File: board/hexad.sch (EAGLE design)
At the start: 0 parts

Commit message: added more parts
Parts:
- added C1, C3: 47uF@50V, holla:C-POLARIZED-E-6
- added C10, C11, C2, C4: 1u, holla:C-0603
- added C5, C7, C8, C9: .1u, holla:C-0603
- added C6: DNP, holla:C-0603
- added D3: VZ10, holla:DIODE-ZENER-SOD323
- added D4: GRN, holla:LED-0603
- added J1, JCYCLE, JDOOR, JFEED: (no value), holla:CONN-02-3.81MM-PLUGIN-SCREW
- added J11: (no value), holla:CONN-MICROSD-2908-05WB-MG
- added J2: (no value), holla:CONN-04-.100-VERT-HEADER
- added J3: (no value), holla:DISP-SPI-TFT-128X160-ST7735
- added JA, JSPINDLE, JX, JY, JZ: (no value), holla:CONN-06-3.81MM-PLUGIN-SCREW
- added JP1, JP2: FIDUCIAL-MICRO, holla:FIDUCIAL-MICRO
- added Q1: 40V, holla:FET-PCH-SOT23
- added Q10, Q11, Q12, Q13, Q2, Q3, Q4, Q5, Q6, Q7, Q8, Q9: (no value), holla:FET-NCH-SOT23
- added R1: 100k, holla:R-0603
- added R10, R12, R16, R20, R22, R4, R7: 10k, holla:R-0603
- added R11, R15, R19, R21, R5, R8, R9: 100, holla:R-0603
- added R13, R14: 2k, holla:R-0603
- added R17, R18: DNP, holla:R-0603
- added R2, R3: (no value), holla:R-0603
- added R23, R6: 1k, holla:R-0603
- added S1: (no value), holla:SWITCH-PUSHBUTTON-EVQ5
- added TP1, TP2, TP3, TPG: (no value), holla:TESTPOINTTHRU
- added U1: RADIO-ESP32_DEVKIT, holla:RADIO-ESP32_DEVKIT
- added U2: R-78E5.0-1.0, holla:VREG-SIP3
- added U3: (no value), holla:IO-MCP23017SO
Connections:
- new net 24V0: C1.+, D3.C, JA.6, JSPINDLE.6, JX.6, JY.6, JZ.6, Q1.S, U2.VIN
- new net 3V3: C10.2, C2.2, C4.2, J11.VDD, Q2.G, R10.2, R12.2, R13.2, R14.2, R16.2, R18.2, R20.2, R22.2, R23.2, R3.2, R4.2, R7.2, U1.3V3, U3.VDD
- new net 5V0: C3.+, JA.5, JSPINDLE.5, JX.5, JY.5, JZ.5, R2.2, R6.2, U1.VIN, U2.VOUT
- new net A_DIR: Q10.G, U1.D2
- new net A_LIMIT: C9.1, R11.2, U1.D4
- new net A_STEP: Q9.G, U1.D15
- new net CS_SD: J11.CS, U1.D34
- new net CYCLE_START: R21.2, U1.VN/AD3/D39
- new net DOOR: R15.2
- new net FEED_HOLD: R19.2, U1.VP/AD0/D36
- new net GND: C1.-, C10.1, C11.1, C2.1, C3.-, C4.1, C5.2, C6.2, C7.2, C8.2, C9.2, D4.C, J1.1, J11.GND, J11.GND1, J11.VSS, J3.GND, JA.1, JCYCLE.1, JDOOR.1, JFEED.1, JSPINDLE.1, JX.1, JY.1, JZ.1, Q10.S, Q11.S, Q12.S, Q13.S, Q3.S, Q4.S, Q5.S, Q6.S, Q7.S, Q8.S, Q9.S, R1.1, S1.1, TPG.P$1, U1.GND@1, U1.GND@2, U2.GND, U3.A0, U3.A1, U3.A2, U3.VSS
- new net MISO: J11.DATA_OUT, TP2.P$1, U1.D19
- new net MOSI: J11.DATA_IN, TP1.P$1, U1.D23
- new net N$1: J1.2, Q1.D
- new net N$10: JA.4, R11.1, R12.1
- new net N$11: JA.2, Q10.D
- new net N$12: JDOOR.2, R15.1, R16.1
- new net N$13: JSPINDLE.4, Q13.D, R17.1, R18.1
- new net N$14: JSPINDLE.2, Q12.D
- new net N$15: J3.RESET
- new net N$16: JFEED.2, R19.1, R20.1
- new net N$17: JCYCLE.2, R21.1, R22.1
- new net N$18: J2.4
- new net N$19: J2.3
- new net N$2: JX.4, R4.1, R8.1
- new net N$20: J2.2
- new net N$21: J2.1
- new net N$22: J3.MOSI
- new net N$23: J3.SCLK
- new net N$24: D3.A, Q1.G, R1.2
- new net N$25: J3.VCC
- new net N$26: J3.CS
- new net N$3: Q2.S, R3.1
- new net N$4: Q2.D, R2.1
- new net N$5: JX.2, Q4.D
- new net N$6: JY.4, R5.1, R7.1
- new net N$7: JY.2, Q6.D
- new net N$8: JZ.4, R10.1, R9.1
- new net N$84: D4.A, R6.1
- new net N$9: JZ.2, Q8.D
- new net RESET: C11.2, R23.1, S1.2, U1.EN, U3.!RESET
- new net SCK: J11.SCLK, TP3.P$1, U1.D18
- new net SCL: R14.1, U1.D22, U3.SCL
- new net SDA: R13.1, U1.D21, U3.SDA
- new net SPINDLE_DIR: Q12.G, U1.D17/TX2
- new net SPINDLE_ENABLE: C6.1, Q13.G, R17.2, U1.D5
- new net SPINDLE_PWM: Q11.G, U1.D16/RX2
- new net X_DIR: Q4.G, U1.D12
- new net X_LIMIT: C5.1, R8.2, U1.D14
- new net X_STEP: Q3.G, U1.D13
- new net X_STEP_5V0: JX.3, Q3.D
- new net X_STEP_5V1: JY.3, Q5.D
- new net X_STEP_5V2: JZ.3, Q7.D
- new net X_STEP_5V3: JA.3, Q9.D
- new net X_STEP_5V4: JSPINDLE.3, Q11.D
- new net Y_DIR: Q6.G, U1.D26
- new net Y_LIMIT: C7.1, R5.2, U1.D25
- new net Y_STEP: Q5.G, U1.D27
- new net Z_DIR: Q8.G, U1.D32
- new net Z_LIMIT: C8.1, R9.2, U1.D35
- new net Z_STEP: Q7.G, U1.D33
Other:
- note added: "add ST7735 display connector"

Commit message: started routing
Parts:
- removed J3: (no value), holla:DISP-SPI-TFT-128X160-ST7735
- removed JDOOR: (no value), holla:CONN-02-3.81MM-PLUGIN-SCREW
- removed S1: (no value), holla:SWITCH-PUSHBUTTON-EVQ5
- removed TP1, TP2, TP3: (no value), holla:TESTPOINTTHRU
- added 24V0, 3V3, 5V0, MISO, MOSI, SCK: (no value), holla:TESTPOINTTHRU
- added C12, C13, C14, C15: .1u, holla:C-0603
- added DISPLAY: (no value), holla:DISP-SPI-TFT-128X160-ST7735
- added J24V0, J3V3, J5V0, LED0, LED1, LED2, LED3, RESET, USER0, USER1, USER2, USER3: (no value), holla:CONN-02-.100-VERT-HEADER
- added R24, R25: 220, holla:R-0603
- added R26, R27: 100, holla:R-0603
- Q1: device holla:FET-PCH-SOT23 -> holla:FET-PCH-TO252
- R15: value 100 -> 220
- R16: value 10k -> 220
- renumbered J1 to VIN, J2 to I2C, JA to A, JCYCLE to CYCLE, JFEED to FEED, JSPINDLE to SPINDLE, JX to X, JY to Y, JZ to Z
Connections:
- removed net DOOR: R15.2
- removed net N$21: I2C.1
- new net DISPLAY_CS: DISPLAY.CS, U3.GPA4
- new net DISPLAY_DC: DISPLAY.DC, U3.GPA5
- new net N$27: LED2.2, R24.2
- new net N$28: LED1.2, R16.2
- new net N$29: LED0.2, R15.2
- new net USER0: C12.1, U3.GPB0, USER0.2
- new net USER1: C13.1, U3.GPB1, USER1.2
- new net USER2: C14.1, U3.GPB2, USER2.2
- new net USER3: C15.1, U3.GPB3, USER3.2
- net 24V0: now also 24V0.P$1, J24V0.2
- net 3V3: now also 3V3.P$1, J3V3.2; no longer R16.2
- net 5V0: now also 5V0.P$1, I2C.2, J5V0.2
- net GND: now also C12.2, C13.2, C14.2, C15.2, DISPLAY.GND, I2C.1, J24V0.1, J3V3.1, J5V0.1, LED0.1, LED1.1, LED2.1, LED3.1, RESET.1, USER0.1, USER1.1, USER2.1, USER3.1; no longer J3.GND, JDOOR.1, S1.1
- net MISO: now also MISO.P$1; no longer TP2.P$1
- net MOSI: now also DISPLAY.MOSI, MOSI.P$1; no longer TP1.P$1
- net N$12: now also U3.GPA0; no longer JDOOR.2, R16.1
- net N$15: now also R16.1, U3.GPA1; no longer J3.RESET
- net N$18: now also R27.1
- net N$19: now also R26.1
- net N$20: now also DISPLAY.BL; no longer I2C.2
- net N$22: now also R24.1, U3.GPA2; no longer J3.MOSI
- net N$23: now also R25.1, U3.GPA3; no longer J3.SCLK
- net N$25: now also DISPLAY.VCC; no longer J3.VCC
- net N$26: now also LED3.2, R25.2; no longer J3.CS
- net RESET: now also DISPLAY.RESET, RESET.2; no longer S1.2
- net SCK: now also DISPLAY.SCLK, SCK.P$1; no longer TP3.P$1
- net SCL: now also R27.2
- net SDA: now also R26.2
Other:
- note removed: "add ST7735 display connector"
- moved on the sheet: C11, R15, R16, R23, U1, U3

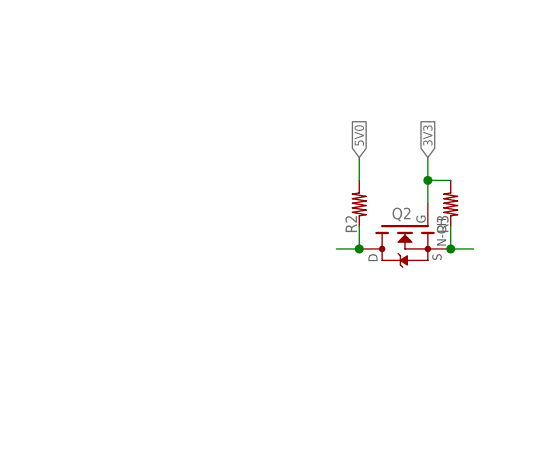
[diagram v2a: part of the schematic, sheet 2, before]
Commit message: changed connectors to 0.1 headers
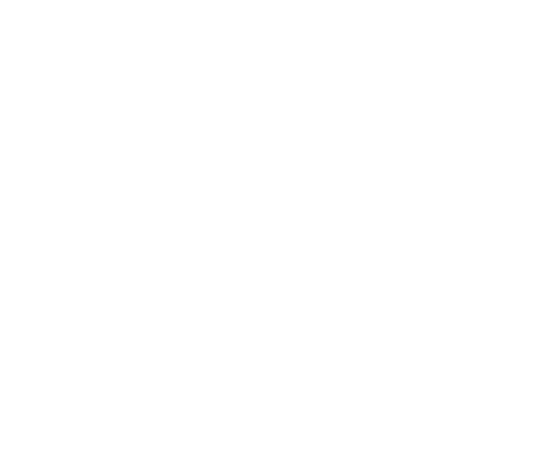
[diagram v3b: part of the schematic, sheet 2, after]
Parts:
- removed 24V0, 5V0: (no value), holla:TESTPOINTTHRU
- removed Q2: (no value), holla:FET-NCH-SOT23
- removed R2, R3: (no value), holla:R-0603
- A, SPINDLE, X, Y, Z: device holla:CONN-06-3.81MM-PLUGIN-SCREW -> holla:CONN-06-.100-VERT-HEADER
- CYCLE, FEED: device holla:CONN-02-3.81MM-PLUGIN-SCREW -> holla:CONN-02-.100-VERT-HEADER
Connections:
- removed net N$3: Q2.S, R3.1
- removed net N$4: Q2.D, R2.1
- net 24V0: no longer 24V0.P$1
- net 3V3: no longer Q2.G, R3.2
- net 5V0: no longer 5V0.P$1, R2.2
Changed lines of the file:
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@@
 <part name="GND2" library="holla" deviceset="GND" device=""/>
 <part name="GND4" library="holla" deviceset="GND" device=""/>
-<part name="X" library="holla" deviceset="CONN-06" device="-3.81MM-PLUGIN-SCREW"/>
-<part name="Q2" library="holla" deviceset="FET-NCH" device="-SOT23"/>
-<part name="R2" library="holla" deviceset="R" device="-0603"/>
-<part name="R3" library="holla" deviceset="R" device="-0603"/>
+<part name="X" library="holla" deviceset="CONN-06" device="-.100-VERT-HEADER"/>
 <part name="FRAME2" library="holla" deviceset="FRAME_A_L" device=""/>
 <part name="GND48" library="holla" deviceset="GND" device=""/>
@@
 <part name="R4" library="holla" deviceset="R" device="-0603" value="10k"/>
 <part name="GND5" library="holla" deviceset="GND" device=""/>
-<part name="Y" library="holla" deviceset="CONN-06" device="-3.81MM-PLUGIN-SCREW"/>
+<part name="Y" library="holla" deviceset="CONN-06" device="-.100-VERT-HEADER"/>
 <part name="R5" library="holla" deviceset="R" device="-0603" value="100"/>
 <part name="Q5" library="holla" deviceset="FET-NCH" device="-SOT23"/>
@@
 <part name="R7" library="holla" deviceset="R" device="-0603" value="10k"/>
 <part name="GND11" library="holla" deviceset="GND" device=""/>
-<part name="Z" library="holla" deviceset="CONN-06" device="-3.81MM-PLUGIN-SCREW"/>
+<part name="Z" library="holla" deviceset="CONN-06" device="-.100-VERT-HEADER"/>
 <part name="R9" library="holla" deviceset="R" device="-0603" value="100"/>
 <part name="Q7" library="holla" deviceset="FET-NCH" device="-SOT23"/>
@@
 <part name="R10" library="holla" deviceset="R" device="-0603" value="10k"/>
 <part name="GND14" library="holla" deviceset="GND" device=""/>
-<part name="A" library="holla" deviceset="CONN-06" device="-3.81MM-PLUGIN-SCREW"/>
+<part name="A" library="holla" deviceset="CONN-06" device="-.100-VERT-HEADER"/>
 <part name="R11" library="holla" deviceset="R" device="-0603" value="100"/>
 <part name="Q9" library="holla" deviceset="FET-NCH" device="-SOT23"/>
@@
 <part name="GND17" library="holla" deviceset="GND" device=""/>
 <part name="GND18" library="holla" deviceset="GND" device=""/>
-<part name="SPINDLE" library="holla" deviceset="CONN-06" device="-3.81MM-PLUGIN-SCREW"/>
+<part name="SPINDLE" library="holla" deviceset="CONN-06" device="-.100-VERT-HEADER"/>
 <part name="R17" library="holla" deviceset="R" device="-0603" value="DNP"/>
 <part name="Q11" library="holla" deviceset="FET-NCH" device="-SOT23"/>
@@
 <part name="GND21" library="holla" deviceset="GND" device=""/>
 <part name="GND22" library="holla" deviceset="GND" device=""/>
-<part name="FEED" library="holla" deviceset="CONN-02" device="-3.81MM-PLUGIN-SCREW"/>
+<part name="FEED" library="holla" deviceset="CONN-02" device="-.100-VERT-HEADER"/>
 <part name="R19" library="holla" deviceset="R" device="-0603" value="100"/>
 <part name="R20" library="holla" deviceset="R" device="-0603" value="10k"/>
 <part name="GND23" library="holla" deviceset="GND" device=""/>
-<part name="CYCLE" library="holla" deviceset="CONN-02" device="-3.81MM-PLUGIN-SCREW"/>
+<part name="CYCLE" library="holla" deviceset="CONN-02" device="-.100-VERT-HEADER"/>
 <part name="R21" library="holla" deviceset="R" device="-0603" value="100"/>
 <part name="R22" library="holla" deviceset="R" device="-0603" value="10k"/>
@@
 <part name="GND32" library="holla" deviceset="GND" device=""/>
 <part name="3V3" library="holla" deviceset="TESTPOINT" device="THRU"/>
-<part name="24V0" library="holla" deviceset="TESTPOINT" device="THRU"/>
-<part name="5V0" library="holla" deviceset="TESTPOINT" device="THRU"/>
 <part name="GND33" library="holla" deviceset="GND" device=""/>
 <part name="GND34" library="holla" deviceset="GND" device=""/>
@@
 <instance part="GND31" gate="1" x="88.9" y="182.88"/>
 <instance part="3V3" gate="G$1" x="236.22" y="200.66"/>
-<instance part="24V0" gate="G$1" x="40.64" y="200.66"/>
-<instance part="5V0" gate="G$1" x="60.96" y="200.66"/>
 <instance part="J24V0" gate="G$1" x="27.94" y="165.1"/>
 <instance part="J5V0" gate="G$1" x="27.94" y="157.48"/>
@@
 <wire x1="60.96" y1="198.12" x2="60.96" y2="195.58" width="0.1524" layer="91"/>
 <junction x="60.96" y="198.12"/>
-<pinref part="5V0" gate="G$1" pin="P$1"/>
 </segment>
 <segment>
@@
 <wire x1="35.56" y1="198.12" x2="35.56" y2="200.66" width="0.1524" layer="91"/>
 <label x="35.56" y="200.66" size="1.016" layer="95" rot="R90" xref="yes"/>
-<pinref part="24V0" gate="G$1" pin="P$1"/>
 </segment>
 <segment>
@@
 <instance part="GND4" gate="1" x="35.56" y="180.34"/>
 <instance part="X" gate="G$1" x="27.94" y="190.5"/>
-<instance part="Q2" gate="G$1" x="205.74" y="182.88" rot="MR270"/>
-<instance part="R2" gate="G$1" x="200.66" y="185.42" rot="R90"/>
-<instance part="R3" gate="G$1" x="210.82" y="185.42" rot="R90"/>
 <instance part="R8" gate="G$1" x="55.88" y="187.96"/>
 <instance part="Q3" gate="G$1" x="55.88" y="177.8" rot="MR0"/>
@@
 </segment>
 <segment>
-<pinref part="R2" gate="G$1" pin="2"/>
-<wire x1="200.66" y1="187.96" x2="200.66" y2="190.5" width="0.1524" layer="91"/>
-<label x="200.66" y="190.5" size="1.016" layer="95" rot="R90" xref="yes"/>
-</segment>
-<segment>
 <pinref part="Y" gate="G$1" pin="5"/>
 <wire x1="33.02" y1="152.4" x2="35.56" y2="152.4" width="0.1524" layer="91"/>
@@
 <net name="3V3" class="0">
 <segment>
-<pinref part="Q2" gate="G$1" pin="G"/>
-<wire x1="208.28" y1="185.42" x2="208.28" y2="187.96" width="0.1524" layer="91"/>
-<pinref part="R3" gate="G$1" pin="2"/>
-<wire x1="208.28" y1="187.96" x2="208.28" y2="190.5" width="0.1524" layer="91"/>
-<wire x1="210.82" y1="187.96" x2="208.28" y2="187.96" width="0.1524" layer="91"/>
-<label x="208.28" y="190.5" size="1.016" layer="95" rot="R90" xref="yes"/>
-<junction x="208.28" y="187.96"/>
-</segment>
-<segment>
 <pinref part="R4" gate="G$1" pin="2"/>
 <wire x1="50.8" y1="195.58" x2="50.8" y2="198.12" width="0.1524" layer="91"/>
@@
 </segment>
 </net>
-<net name="N$3" class="0">
-<segment>
-<pinref part="Q2" gate="G$1" pin="S"/>
-<pinref part="R3" gate="G$1" pin="1"/>
-<wire x1="210.82" y1="180.34" x2="213.36" y2="180.34" width="0.1524" layer="91"/>
-<wire x1="210.82" y1="182.88" x2="210.82" y2="180.34" width="0.1524" layer="91"/>
-<junction x="210.82" y="180.34"/>
-</segment>
-</net>
-<net name="N$4" class="0">
-<segment>
-<pinref part="Q2" gate="G$1" pin="D"/>
-<wire x1="200.66" y1="180.34" x2="198.12" y2="180.34" width="0.1524" layer="91"/>
-<pinref part="R2" gate="G$1" pin="1"/>
-<wire x1="200.66" y1="180.34" x2="200.66" y2="182.88" width="0.1524" layer="91"/>
-<junction x="200.66" y="180.34"/>
-</segment>
-</net>

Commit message: release v1.0
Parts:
- removed Q13: (no value), holla:FET-NCH-SOT23
- added Q2: (no value), holla:FET-NCH-SOT23
- added R2, R3: 220, holla:R-0603
- C1: value 47uF@50V -> 1u; device holla:C-POLARIZED-E-6 -> holla:C-0603
- C10, C11, C4: value 1u -> .1u
- C13, C9: value .1u -> 1u
- C14, C15: value .1u -> 47uF@50V; device holla:C-0603 -> holla:C-POLARIZED-E-6
- C3: value 47uF@50V -> .1u; device holla:C-POLARIZED-E-6 -> holla:C-0603
- C6: value DNP -> .1u
- C7: value .1u -> DNP
- R1: value 100k -> 2k
- R10, R12, R22: value 10k -> 100
- R13: value 2k -> 10k
- R14: value 2k -> 100
- R15: value 220 -> 10k
- R16: value 220 -> 1k
- R17: value DNP -> 100k
- R18: value DNP -> 10k
- R23: value 1k -> 10k
- R24, R25: value 220 -> DNP
- R26: value 100 -> 10k
- R4: value 10k -> 220
- R5: value 100 -> 220
- R7: value 10k -> 2k
- U1: value RADIO-ESP32_DEVKIT -> (none); device holla:RADIO-ESP32_DEVKIT -> holla:IO-MCP23017SO
- U2: value R-78E5.0-1.0 -> RADIO-ESP32_DEVKIT; device holla:VREG-SIP3 -> holla:RADIO-ESP32_DEVKIT
- U3: value (none) -> R-78E5.0-1.0; device holla:IO-MCP23017SO -> holla:VREG-SIP3
- renumbered D3 to D2, D4 to D1, J11 to J1, JP1 to FID1, JP2 to FID2, TPG to GND
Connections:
- removed net N$25: DISPLAY.VCC
- new net N$3: DISPLAY.SCLK, R9.1
- new net N$4: DISPLAY.MOSI, R8.1
- net 24V0: now also C14.+, U3.VIN; no longer C1.+, U2.VIN
- net 3V3: now also C1.2, C13.2, C9.2, R1.2, R15.2, R25.2, R26.2, R6.2, U1.VDD, U2.3V3; no longer C10.2, C2.2, C4.2, R10.2, R12.2, R14.2, R22.2, R4.2, U1.3V3, U3.VDD
- net 5V0: now also C15.+, DISPLAY.VCC, R16.2, U2.VIN, U3.VOUT; no longer C3.+, R6.2, U1.VIN, U2.VOUT
- net A_DIR: now also Q6.G, U2.D2; no longer Q10.G, U1.D2
- net A_LIMIT: now also C11.1, R22.2, U2.D4; no longer C9.1, R11.2, U1.D4
- net A_STEP: now also Q7.G, U2.D15; no longer Q9.G, U1.D15
- net CS_SD: now also U2.D34; no longer U1.D34
- net CYCLE_START: now also R14.2, U2.VN/AD3/D39; no longer R21.2, U1.VN/AD3/D39
- net DISPLAY_CS: now also U1.GPA4; no longer U3.GPA4
- net DISPLAY_DC: now also U1.GPA5; no longer U3.GPA5
- net FEED_HOLD: now also R12.2, U2.VP/AD0/D36; no longer R19.2, U1.VP/AD0/D36
- net GND: now also C1.1, C10.2, C11.2, C13.1, C14.-, C15.-, C3.2, C4.2, C9.1, Q2.S, R17.1, U1.A0, U1.A1, U1.A2, U1.VSS, U2.GND@1, U2.GND@2, U3.GND; no longer C1.-, C10.1, C11.1, C13.2, C14.2, C15.2, C3.-, C4.1, C9.2, Q13.S, R1.1, U1.GND@1, U1.GND@2, U2.GND, U3.A0, U3.A1, U3.A2, U3.VSS
- net MISO: now also U2.D19; no longer U1.D19
- net MOSI: now also R8.2, U2.D23; no longer DISPLAY.MOSI, U1.D23
- net N$10: now also R22.1, R23.1; no longer R11.1, R12.1
- net N$11: now also Q6.D; no longer Q10.D
- net N$12: now also R5.1, U1.GPA0; no longer R15.1, U3.GPA0
- net N$13: now also Q9.D, R24.1, R25.1; no longer Q13.D, R17.1, R18.1
- net N$14: now also Q10.D; no longer Q12.D
- net N$15: now also R4.1, U1.GPA1; no longer R16.1, U3.GPA1
- net N$16: now also R12.1, R13.1; no longer R19.1, R20.1
- net N$17: now also R14.1, R15.1; no longer R21.1, R22.1
- net N$18: now also R10.1; no longer R27.1
- net N$19: now also R11.1; no longer R26.1
- net N$2: now also R26.1, R27.1; no longer R4.1, R8.1
- net N$22: now also R3.1, U1.GPA2; no longer R24.1, U3.GPA2
- net N$23: now also R2.1, U1.GPA3; no longer R25.1, U3.GPA3
- net N$24: now also R17.2; no longer R1.2
- net N$26: now also R2.2; no longer R25.2
- net N$27: now also R3.2; no longer R24.2
- net N$28: now also R4.2; no longer R16.2
- net N$29: now also R5.2; no longer R15.2
- net N$5: now also Q11.D; no longer Q4.D
- net N$6: now also R19.1, R20.1; no longer R5.1, R7.1
- net N$7: now also Q2.D; no longer Q6.D
- net N$8: now also R18.1, R21.1; no longer R10.1, R9.1
- net N$84: now also R16.1; no longer R6.1
- net N$9: now also Q4.D; no longer Q8.D
- net RESET: now also C2.2, R6.1, U1.!RESET, U2.EN; no longer C11.2, R23.1, U1.EN, U3.!RESET
- net SCK: now also R9.2, U2.D18; no longer DISPLAY.SCLK, U1.D18
- net SCL: now also R1.1, R10.2, U1.SCL, U2.D22; no longer R14.1, R27.2, U1.D22, U3.SCL
- net SDA: now also R11.2, R7.1, U1.SDA, U2.D21; no longer R13.1, R26.2, U1.D21, U3.SDA
- net SPINDLE_DIR: now also Q10.G, U2.D16/RX2; no longer Q12.G, U1.D17/TX2
- net SPINDLE_ENABLE: now also C7.1, Q9.G, R24.2, U2.D5; no longer C6.1, Q13.G, R17.2, U1.D5
- net SPINDLE_PWM: now also Q8.G, U2.D17/TX2; no longer Q11.G, U1.D16/RX2
- net USER0: now also C3.1, U1.GPB0; no longer C12.1, U3.GPB0
- net USER1: now also C5.1, U1.GPB1; no longer C13.1, U3.GPB1
- net USER2: now also C8.1, U1.GPB2; no longer C14.1, U3.GPB2
- net USER3: now also C12.1, U1.GPB3; no longer C15.1, U3.GPB3
- net X_DIR: now also Q11.G, U2.D12; no longer Q4.G, U1.D12
- net X_LIMIT: now also C10.1, R27.2, U2.D14; no longer C5.1, R8.2, U1.D14
- net X_STEP: now also Q12.G, U2.D13; no longer Q3.G, U1.D13
- net X_STEP_5V0: now also Q12.D; no longer Q3.D
- net X_STEP_5V1: now also Q3.D; no longer Q5.D
- net X_STEP_5V2: now also Q5.D; no longer Q7.D
- net X_STEP_5V3: now also Q7.D; no longer Q9.D
- net X_STEP_5V4: now also Q8.D; no longer Q11.D
- net Y_DIR: now also Q2.G, U2.D26; no longer Q6.G, U1.D26
- net Y_LIMIT: now also C6.1, R19.2, U2.D25; no longer C7.1, R5.2, U1.D25
- net Y_STEP: now also Q3.G, U2.D27; no longer Q5.G, U1.D27
- net Z_DIR: now also Q4.G, U2.D32; no longer Q8.G, U1.D32
- net Z_LIMIT: now also C4.1, R21.2, U2.D35; no longer C8.1, R9.2, U1.D35
- net Z_STEP: now also Q5.G, U2.D33; no longer Q7.G, U1.D33
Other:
- moved on the sheet: C12, C2, C5, C6, C7, C8, Q10, Q11, Q12, Q3, Q4, Q5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
